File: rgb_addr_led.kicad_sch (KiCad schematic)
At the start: 64 parts

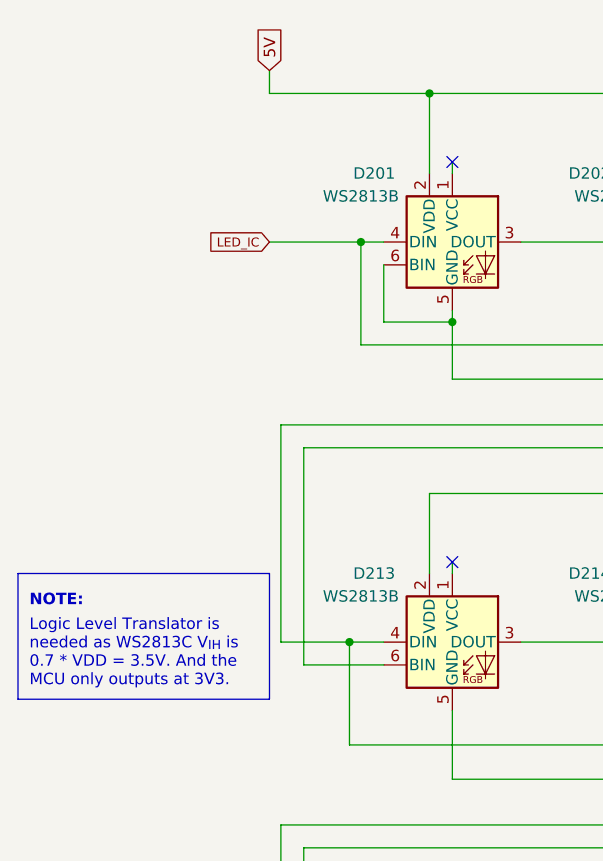
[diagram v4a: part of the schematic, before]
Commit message: update hierarchical labels
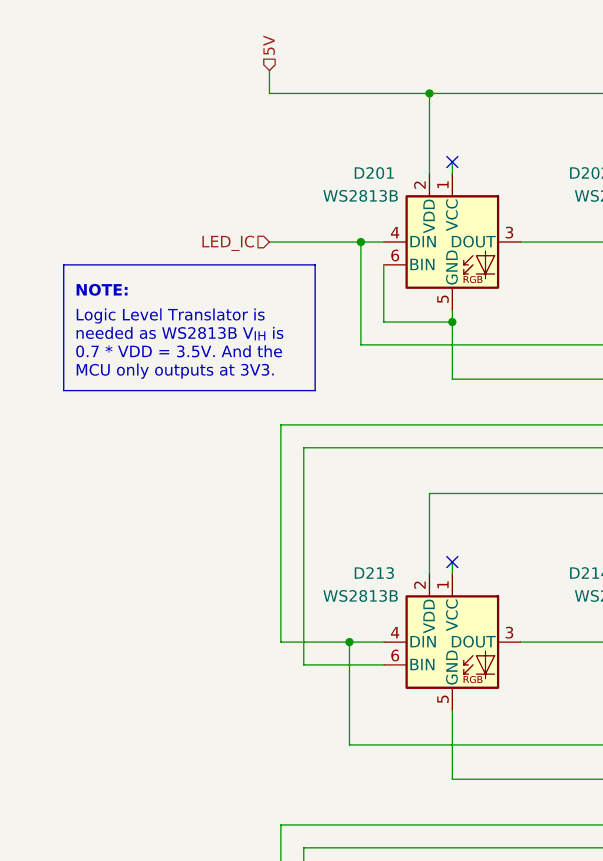
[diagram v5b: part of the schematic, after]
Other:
- note added: "Logic Level Translator is needed as WS2813B V_{IH} is 0.7 * VDD = 3.5V. And the MCU only outputs at 3V3."
- note removed: "Logic Level Translator is needed as WS2813C V_{IH} is 0.7 * VDD = 3.5V. And the MCU only outputs at 3V3."
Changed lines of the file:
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@@
     (stroke (width 0) (type default) (color 0 0 0 0))
   )
-  (polyline (pts (xy 12.7 73.66) (xy 12.7 87.63))
+  (polyline (pts (xy 17.78 39.37) (xy 17.78 53.34))
     (stroke (width 0) (type default) (color 0 0 0 0))
   )
@@
     (stroke (width 0) (type default) (color 0 0 0 0))
   )
-  (polyline (pts (xy 40.64 87.63) (xy 12.7 87.63))
+  (polyline (pts (xy 45.72 53.34) (xy 17.78 53.34))
     (stroke (width 0) (type default) (color 0 0 0 0))
   )
@@
     (stroke (width 0) (type default) (color 0 0 0 0))
   )
-  (polyline (pts (xy 40.64 73.66) (xy 40.64 87.63))
+  (polyline (pts (xy 45.72 39.37) (xy 45.72 53.34))
     (stroke (width 0) (type default) (color 0 0 0 0))
   )
@@
     (stroke (width 0) (type default) (color 0 0 0 0))
   )
-  (polyline (pts (xy 12.7 73.66) (xy 40.64 73.66))
+  (polyline (pts (xy 17.78 39.37) (xy 45.72 39.37))
     (stroke (width 0) (type default) (color 0 0 0 0))
   )
@@
     (stroke (width 0) (type default) (color 0 0 0 0))
   )
-  (text "NOTE:" (at 13.97 77.47 0)
+  (text "NOTE:" (at 19.05 43.18 0)
     (effects (font (size 1.27 1.27) (thickness 0.254) bold) (justify left bottom))
   )
-  (text "\nLogic Level Translator is\nneeded as WS2813C V_{IH} is\n0.7 * VDD = 3.5V. And the\nMCU only outputs at 3V3."
-    (at 13.97 86.36 0)
+  (text "\nLogic Level Translator is\nneeded as WS2813B V_{IH} is\n0.7 * VDD = 3.5V. And the\nMCU only outputs at 3V3."
+    (at 19.05 52.07 0)
     (effects (font (size 1.27 1.27)) (justify left bottom))
   )
-  (global_label "5V" (shape input) (at 40.64 17.78 90) (fields_autoplaced)
+  (hierarchical_label "LED_IC" (shape input) (at 40.64 36.83 180)
+    (effects (font (size 1.27 1.27)) (justify right))
+  )
+  (hierarchical_label "5V" (shape input) (at 40.64 17.78 90)
     (effects (font (size 1.27 1.27)) (justify left))
-    (property "Intersheet References" "${INTERSHEET_REFS}" (id 0) (at 40.5606 13.0688 90)
-      (effects (font (size 1.27 1.27)) (justify left) hide)
-    )
-  )
-  (global_label "LED_IC" (shape input) (at 40.64 36.83 180) (fields_autoplaced)
-    (effects (font (size 1 1)) (justify right))
-    (property "Intersheet References" "${INTERSHEET_REFS}" (id 0) (at 33.7876 36.7675 0)
-      (effects (font (size 1 1)) (justify right) hide)
-    )
   )
   (symbol (lib_id "LED:WS2813") (at 88.9 214.63 0) (unit 1)

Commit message: add caps/resistors back to ws2813b schematic
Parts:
- added C201, C202, C203, C204, C205, C206, C207, C208, C209, C210, C211, C212, C213, C214, C215, C216, C217, C218, C219, C220, C221, C222, C223, C224, C225, C226, C227, C228, C229, C230, C231, C232, C233, C234, C235, C236, C237, C238, C239, C240, C241, C242, C243, C244, C245, C246, C247, C248, C249, C250, C251, C252, C253, C254, C255, C256, C257, C258, C259, C260, C261, C262, C263, C264: 100nF, Capacitor_SMD:C_0603_1608Metric, symbol Device:C_Small
- added R201, R202, R203, R204, R205, R206, R207, R208, R209, R210, R211, R212, R214, R215, R216, R217, R218, R219, R220, R221, R222, R223, R224, R225, R226, R227, R228, R229, R230, R231, R232, R233, R234, R235, R236, R237, R238, R239, R240, R241, R242, R243, R244, R245, R246, R247, R248, R249, R250, R251, R252, R253, R254, R255, R256, R257, R258, R259, R260, R261, R262, R263, R264, R265: 200, Resistor_SMD:R_0603_1608Metric, symbol Device:R_Small
- D201, D202, D203, D204, D205, D206, D207, D208, D209, D210, D211, D212, D213, D214, D215, D216, D217, D218, D219, D220, D221, D222, D223, D224, D225, D226, D227, D228, D229, D230, D231, D232, D233, D234, D235, D236, D237, D238, D239, D240, D241, D242, D243, D244, D245, D246, D247, D248, D249, D250, D251, D252, D253, D254, D255, D256, D257, D258, D259, D260, D261, D262, D263, D264: LCSC C114592 -> C194323
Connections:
- net 5V: now also R201.1, R202.1, R203.1, R204.1, R205.1, R206.1, R207.1, R208.1, R209.1, R210.1, R211.1, R212.1, R214.1, R215.1, R216.1, R217.1, R218.1, R219.1, R220.1, R221.1, R222.1, R223.1, R224.1, R225.1, R226.1, R227.1, R228.1, R229.1, R230.1, R231.1, R232.1, R233.1, R234.1, R235.1, R236.1, R237.1, R238.1, R239.1, R240.1, R241.1, R242.1, R243.1, R244.1, R245.1, R246.1, R247.1, R248.1, R249.1, R250.1, R251.1, R252.1, R253.1, R254.1, R255.1, R256.1, R257.1, R258.1, R259.1, R260.1, R261.1, R262.1, R263.1, R264.1, R265.1
- net GND: now also C201.2, C202.2, C203.2, C204.2, C205.2, C206.2, C207.2, C208.2, C209.2, C210.2, C211.2, C212.2, C213.2, C214.2, C215.2, C216.2, C217.2, C218.2, C219.2, C220.2, C221.2, C222.2, C223.2, C224.2, C225.2, C226.2, C227.2, C228.2, C229.2, C230.2, C231.2, C232.2, C233.2, C234.2, C235.2, C236.2, C237.2, C238.2, C239.2, C240.2, C241.2, C242.2, C243.2, C244.2, C245.2, C246.2, C247.2, C248.2, C249.2, C250.2, C251.2, C252.2, C253.2, C254.2, C255.2, C256.2, C257.2, C258.2, C259.2, C260.2, C261.2, C262.2, C263.2, C264.2
- net at D250.1 (VCC): now also C250.1, R251.2
- net at D257.1 (VCC): now also C257.1, R258.2
- net at D256.1 (VCC): now also C256.1, R257.2
- net at D252.1 (VCC): now also C252.1, R253.2
- net at D210.1 (VCC): now also C210.1, R210.2
- net at D213.1 (VCC): now also C213.1, R214.2
- net at D211.1 (VCC): now also C211.1, R211.2
- net at D219.1 (VCC): now also C219.1, R220.2
- net at D216.1 (VCC): now also C216.1, R217.2
- net at D248.1 (VCC): now also C248.1, R249.2
- net at D233.1 (VCC): now also C233.1, R234.2
- net at D209.1 (VCC): now also C209.1, R209.2
- net at D203.1 (VCC): now also C203.1, R203.2
- net at D202.1 (VCC): now also C202.1, R202.2
- net at D240.1 (VCC): now also C240.1, R241.2
- net at D228.1 (VCC): now also C228.1, R229.2
- net at D204.1 (VCC): now also C204.1, R204.2
- net at D206.1 (VCC): now also C206.1, R206.2
- net at D231.1 (VCC): now also C231.1, R232.2
- net at D255.1 (VCC): now also C255.1, R256.2
- net at D226.1 (VCC): now also C226.1, R227.2
- net at D261.1 (VCC): now also C261.1, R262.2
- net at D235.1 (VCC): now also C235.1, R236.2
- net at D260.1 (VCC): now also C260.1, R261.2
- net at D207.1 (VCC): now also C207.1, R207.2
- net at D225.1 (VCC): now also C225.1, R226.2
- net at D239.1 (VCC): now also C239.1, R240.2
- net at D245.1 (VCC): now also C245.1, R246.2
- net at D218.1 (VCC): now also C218.1, R219.2
- net at D222.1 (VCC): now also C222.1, R223.2
- net at D217.1 (VCC): now also C217.1, R218.2
- net at D238.1 (VCC): now also C238.1, R239.2
- net at D232.1 (VCC): now also C232.1, R233.2
- net at D249.1 (VCC): now also C249.1, R250.2
- net at D230.1 (VCC): now also C230.1, R231.2
- net at D259.1 (VCC): now also C259.1, R260.2
- net at D227.1 (VCC): now also C227.1, R228.2
- net at D212.1 (VCC): now also C212.1, R212.2
- net at D237.1 (VCC): now also C237.1, R238.2
- net at D243.1 (VCC): now also C243.1, R244.2
- net at D223.1 (VCC): now also C223.1, R224.2
- net at D264.1 (VCC): now also C264.1, R265.2
- net at D220.1 (VCC): now also C220.1, R221.2
- net at D224.1 (VCC): now also C224.1, R225.2
- net at D208.1 (VCC): now also C208.1, R208.2
- net at D258.1 (VCC): now also C258.1, R259.2
- net at D247.1 (VCC): now also C247.1, R248.2
- net at D251.1 (VCC): now also C251.1, R252.2
- net at D242.1 (VCC): now also C242.1, R243.2
- net at D254.1 (VCC): now also C254.1, R255.2
- net at D263.1 (VCC): now also C263.1, R264.2
- net at D253.1 (VCC): now also C253.1, R254.2
- net at D215.1 (VCC): now also C215.1, R216.2
- net at D229.1 (VCC): now also C229.1, R230.2
- net at D246.1 (VCC): now also C246.1, R247.2
- net at D221.1 (VCC): now also C221.1, R222.2
- net at D205.1 (VCC): now also C205.1, R205.2
- net at D234.1 (VCC): now also C234.1, R235.2
- net at D262.1 (VCC): now also C262.1, R263.2
- net at D244.1 (VCC): now also C244.1, R245.2
- net at D214.1 (VCC): now also C214.1, R215.2
- net at D201.1 (VCC): now also C201.1, R201.2
- net at D236.1 (VCC): now also C236.1, R237.2
- net at D241.1 (VCC): now also C241.1, R242.2
- no-connect marks 65 -> 1
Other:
- note added: "Bus buffer is used as WS2813B V_{IH} is 0.7 * VDD = 3.5V. ESP32 outputs at 3V3."
- note removed: "Logic Level Translator is needed as WS2813B V_{IH} is 0.7 * VDD = 3.5V. And the MCU only outputs at 3V3."
